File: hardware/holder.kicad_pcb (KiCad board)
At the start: 2 copper layers, 80 x 50.5 mm, 1 part

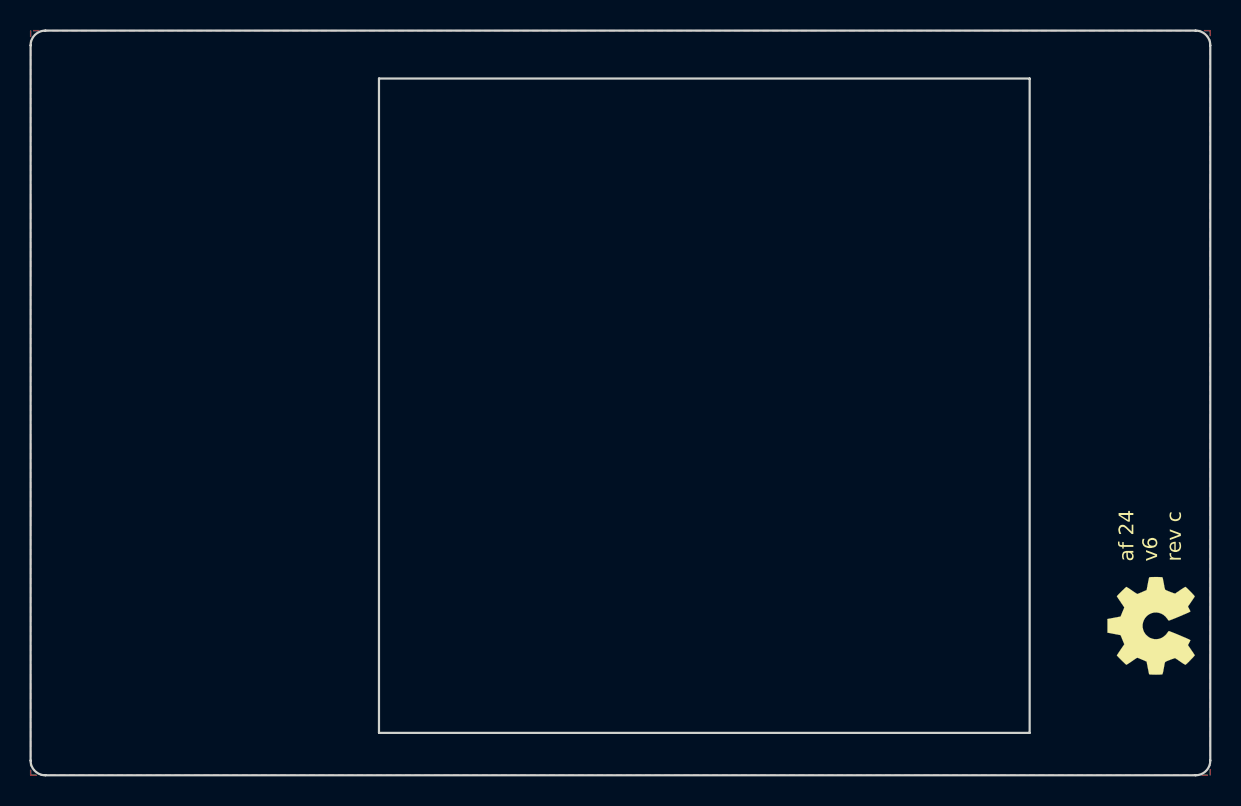
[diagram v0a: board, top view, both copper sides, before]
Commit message: feat: hardware modules for new XLR connector
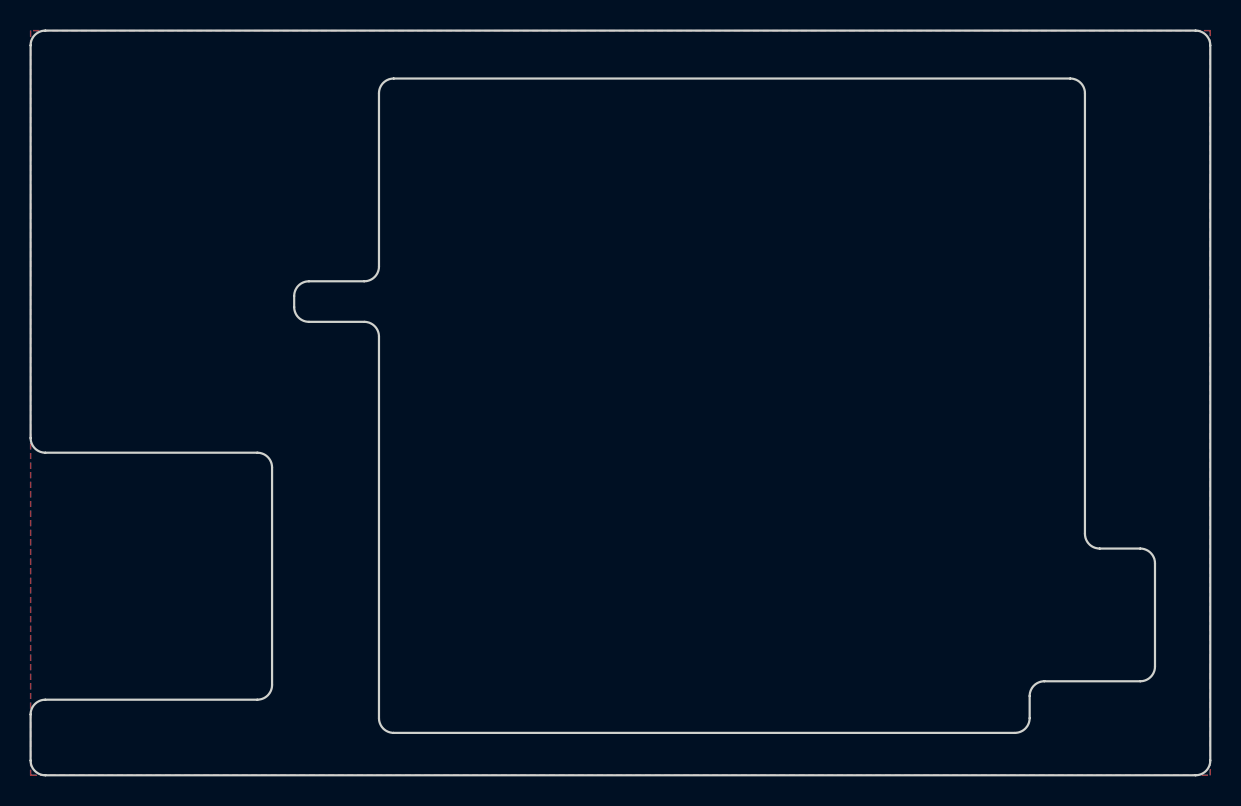
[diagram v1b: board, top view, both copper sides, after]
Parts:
- removed oshw1: Logo_Open_Hardware_Large, Symbol:OSHW-Symbol_6.7x6mm_SilkScreen
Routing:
- added copper zone on B.Cu, net (none)
- added copper zone on F.Cu, net (none)
- removed copper zone on B.Cu, net GND
- removed copper zone on F.Cu, net GND
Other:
- outline, holes or cut-outs redrawn
- board text removed: "af 24 v6 rev c"
- board text removed: "löti"
